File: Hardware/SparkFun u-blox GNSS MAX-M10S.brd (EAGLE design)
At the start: 38.1 x 30.5 mm, 90 parts, among them J1 USB-to-Serial, J2 Qwiic RA, J3 PTH, J4 Qwiic RA, U1 MAX-M10S

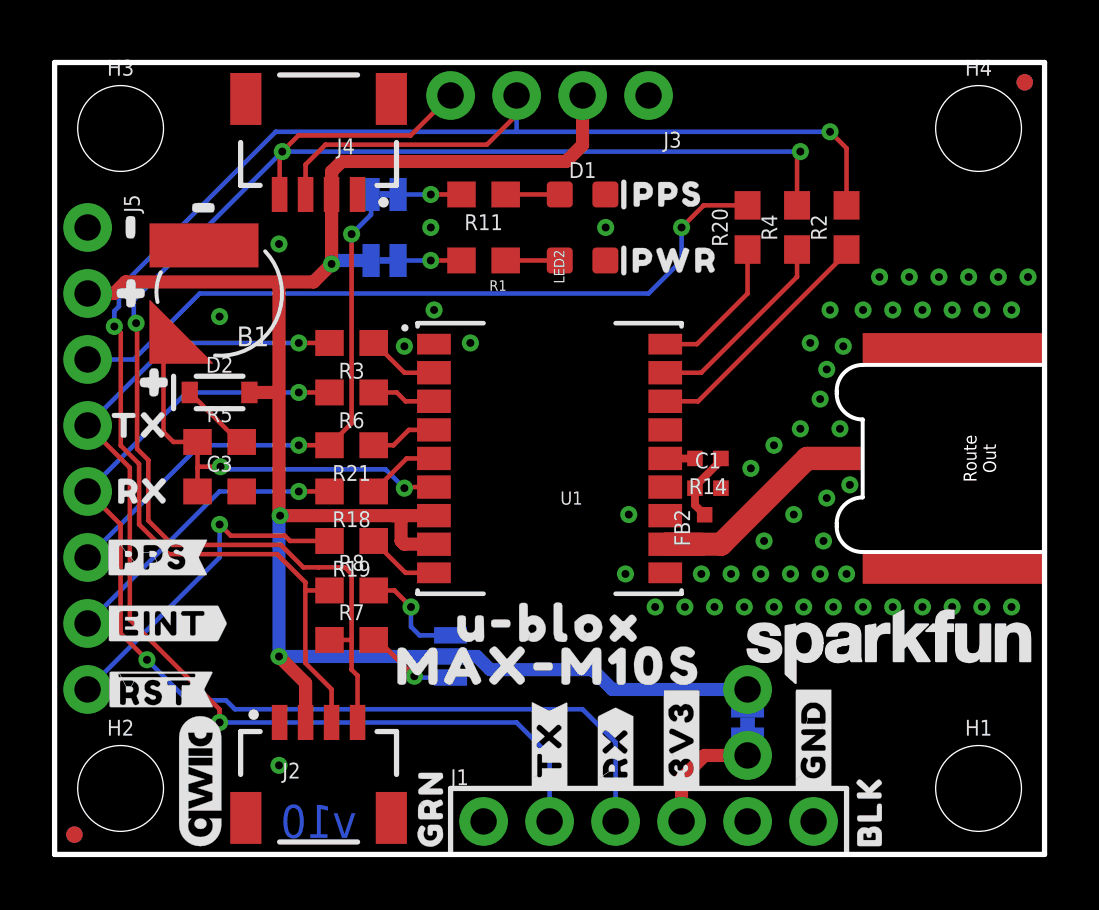
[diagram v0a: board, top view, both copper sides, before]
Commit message: Add ESD RF diode. Change to PTH SMA.
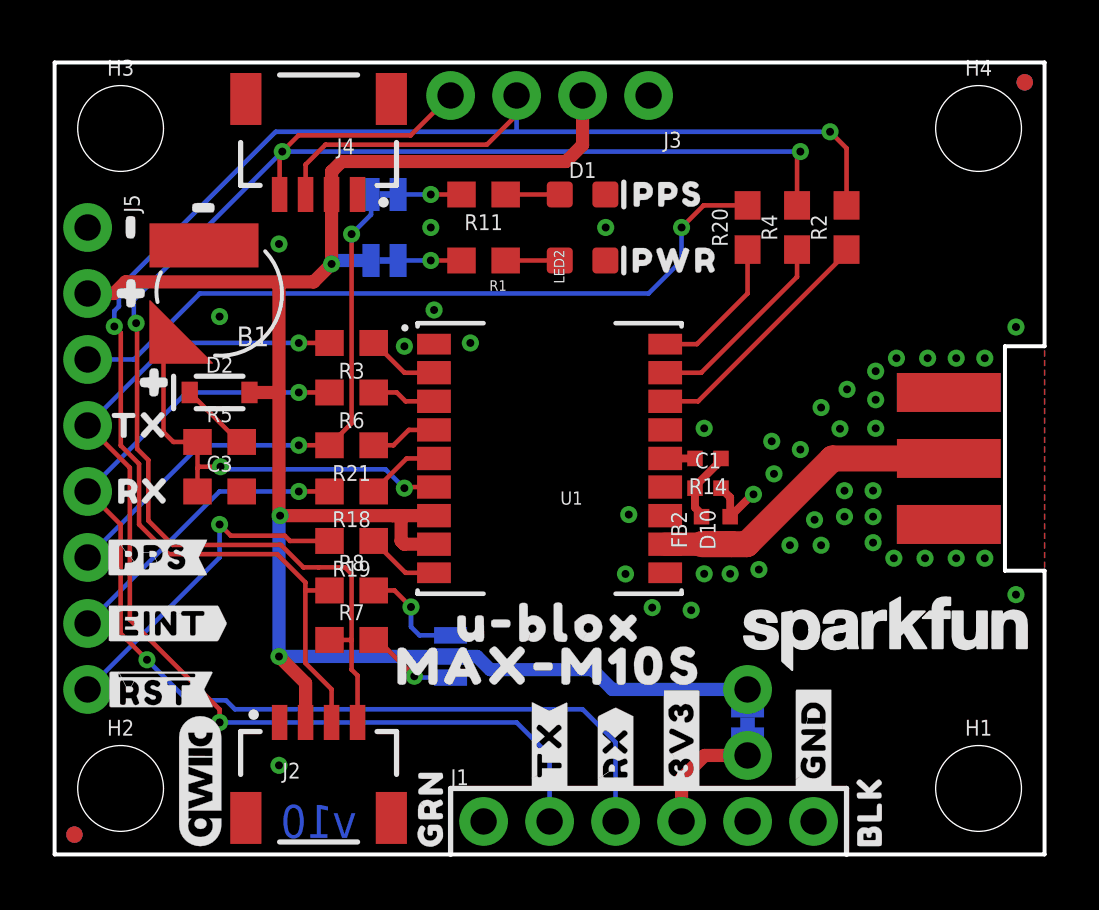
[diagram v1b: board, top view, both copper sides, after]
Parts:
- added D10: PESD0402-0402T, SparkFun-DiscreteSemi:0402-TIGHT
- C1: value 47PF-0402_TIGHT-25V-5%-X7R -> 47pF
- E1: value (none) -> ANTENNA-SMA-GROUNDEDEDGE_SMA; device SparkFun-RF:SMA-EDGE-SMD -> SparkFun-RF:SMA-EDGE
- JP5: value (none) -> JUMPER-SMT_3_NO_SILK
- MEAS: value (none) -> JUMPER-COMBO_2_NC_TRACE
- PPS_LED, PWR: value (none) -> JUMPER-SMT_2_NC_TRACE_SILK
- moved E1 3.68 mm to (34.4, 15.2)
- moved LOGO4 0.52 mm to (32.0, 8.50)
- moved FB2 0.14 mm to (24.9, 12.5)
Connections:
- net GND: now also D10.2, E1.GND@2, E1.GND@3
- net GPS_RF: now also D10.1
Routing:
- net GPS_RF: track 9.44 -> 13.5 mm
- net GND: track 0.00 -> 2.50 mm, vias 55 -> 44
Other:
- outline, holes or cut-outs redrawn

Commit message: Add panel files
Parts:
- moved C1 0.25 mm to (25.4, 14.1)
- moved R14 0.25 mm to (25.4, 15.2)
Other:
- board text added: "Route Out"
